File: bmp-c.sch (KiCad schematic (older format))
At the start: 66 parts, among them J1 USB_C_Receptacle_USB2.0, J2 Conn_01x10, J3 Conn_01x04, J4 JTAG-10, Q1 DMG1023DV, Q2 DMG1024UV, SW1 SW_SPST, U1 USBLC6-2SC6, U2 74LVC2T45DC, U3 74LVC2T45DC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

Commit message: Assign footprints
Signed-off-by: Dominik Sliwa <dominik@e-plum.pl>
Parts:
- C1, C10, C11, C12, C13, C14, C15, C16, C17, C18, C19, C2, C20, C4, C5, C6, C8, C9: footprint (none) -> Capacitor_SMD:C_0402_1005Metric
- C21, C3: footprint (none) -> Capacitor_SMD:C_0603_1608Metric
- C7: footprint (none) -> Capacitor_SMD:C_0201_0603Metric
- D1, Q1, Q2: footprint (none) -> Package_TO_SOT_SMD:SOT-563
- D2, D3, D4: footprint (none) -> LED_SMD:LED_0402_1005Metric
- FB1: footprint (none) -> Fuse:Fuse_0603_1608Metric
- J1: footprint (none) -> Connector_USB:USB_C_Receptacle_HRO_TYPE-C-31-M-12
- J2: footprint (none) -> Connector_FFC-FPC:Hirose_FH12-10S-0.5SH_1x10-1MP_P0.50mm_Horizontal
- J3: footprint (none) -> Connector_JST:JST_SH_SM04B-SRSS-TB_1x04-1MP_P1.00mm_Horizontal
- J4: footprint (none) -> Connector_PinHeader_1.27mm:PinHeader_2x05_P1.27mm_Vertical_SMD
- JP1, JP2, JP3: footprint (none) -> Jumper:SolderJumper-2_P1.3mm_Bridged_RoundedPad1.0x1.5mm
- JP4: footprint (none) -> Jumper:SolderJumper-2_P1.3mm_Open_RoundedPad1.0x1.5mm
- R1, R10, R11, R12, R2, R3, R4, R5, R6, R7, R8, R9: footprint (none) -> Resistor_SMD:R_0402_1005Metric
- RN1, RN2, RN3: footprint (none) -> Resistor_SMD:R_Array_Convex_4x0402
- SW1: footprint (none) -> Button_Switch_SMD:SW_SPST_B3U-1000P
- TP1, TP2, TP3, TP4, TP5, TP6: footprint (none) -> TestPoint:TestPoint_Pad_D1.0mm
- U7: footprint (none) -> Package_DFN_QFN:UDFN-4_1x1mm_P0.65mm
- Y1: footprint (none) -> Crystal:Crystal_SMD_3225-4Pin_3.2x2.5mm

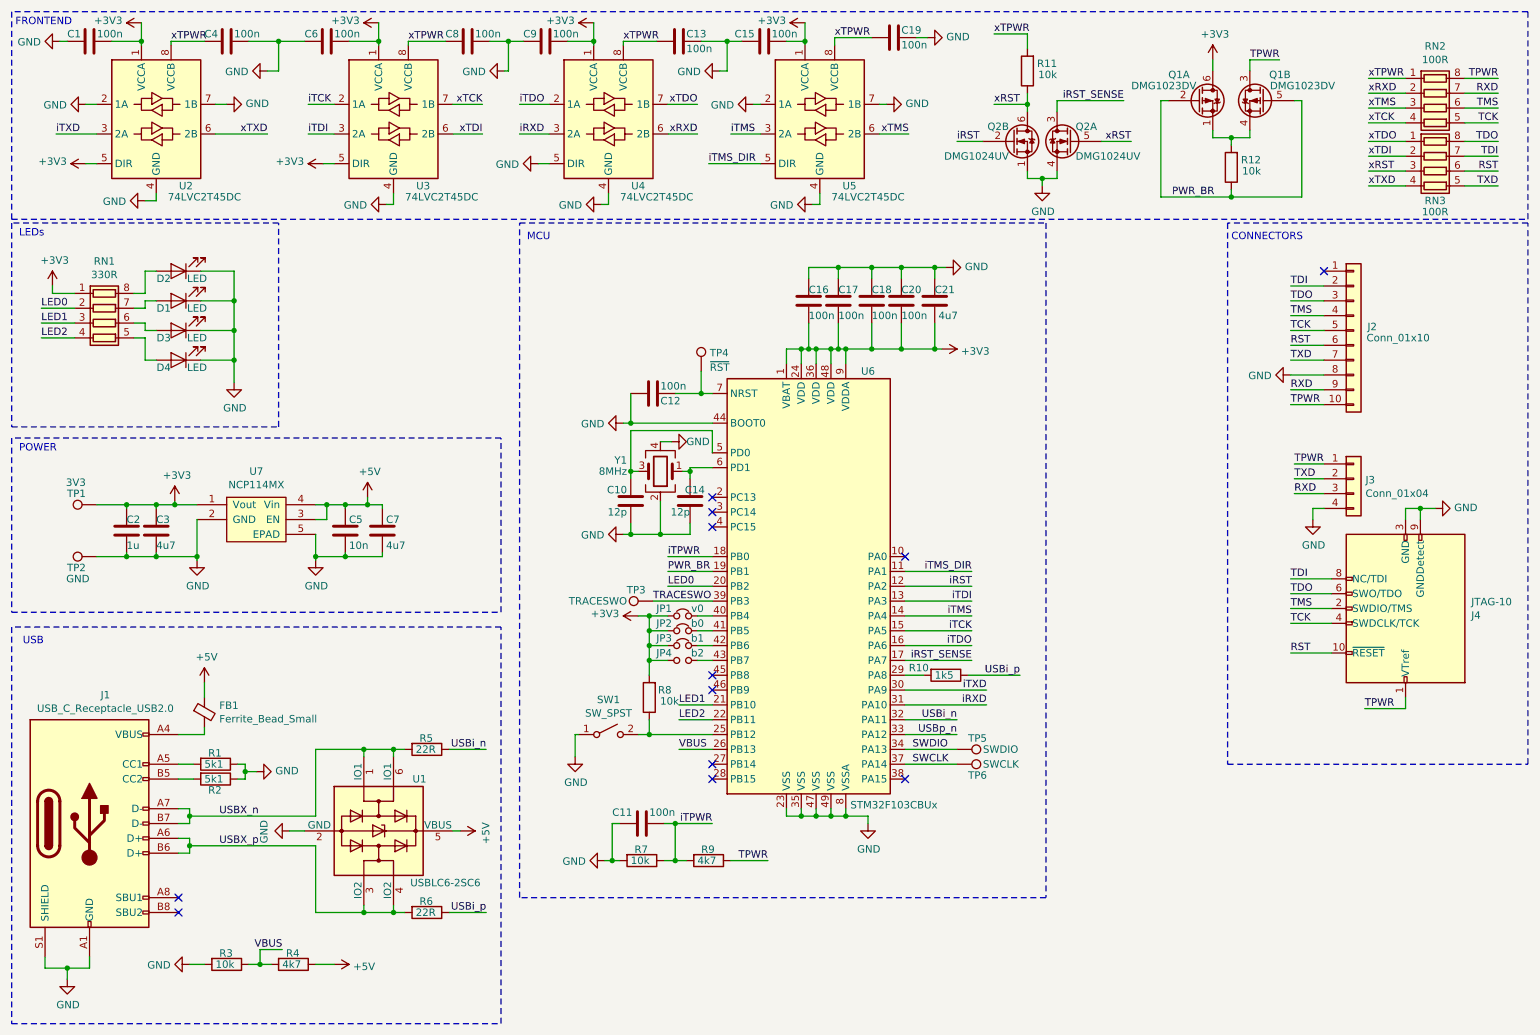
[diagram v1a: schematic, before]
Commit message: Change level-shifter package and schematic fix
-USBi_p was not conencted to the MCU
-Use 74LVC2T45 in the DSBGA8 package

Signed-off-by: Dominik Sliwa <dominik@e-plum.pl>
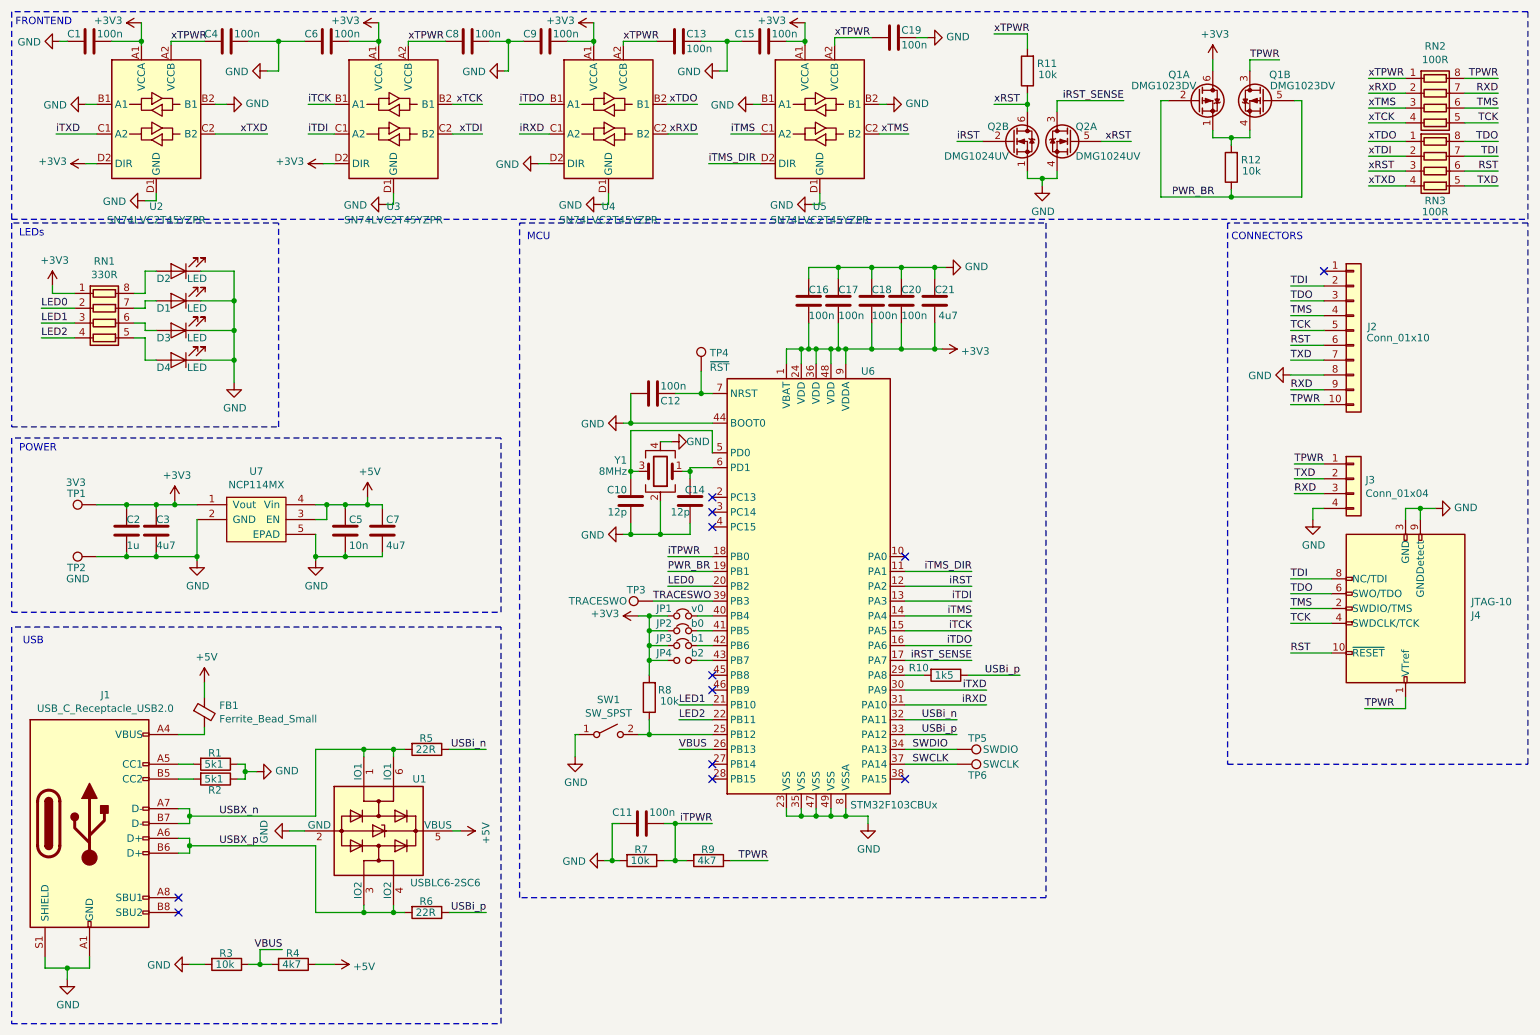
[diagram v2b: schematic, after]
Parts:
- removed U2, U3, U4, U5: 74LVC2T45DC, Package_SO:VSSOP-8_2.3x2mm_P0.5mm, symbol Logic_LevelTranslator:74LVC2T45DC
- added U2, U3, U4, U5: SN74LVC2T45YZPR, Package_BGA:Texas_DSBGA-8_0.9x1.9mm_Layout2x4_P0.5mm, symbol Logic_LevelTranslator:SN74LVC2T45YZPR
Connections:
- net USBp_n is gone; now on net USBi_p: U6.33 (PA12)
- net +3V3: now also U2.A1 (VCCA), U2.D2 (DIR), U3.A1 (VCCA), U3.D2 (DIR), U4.A1 (VCCA), U5.A1 (VCCA)
- net GND: now also U2.B1 (A1), U2.B2 (B1), U2.D1 (GND), U3.D1 (GND), U4.D1 (GND), U4.D2 (DIR), U5.B1 (A1), U5.B2 (B1), U5.D1 (GND)
- net iRXD: now also U4.C1 (A2)
- net iTCK: now also U3.B1 (A1)
- net iTDI: now also U3.C1 (A2)
- net iTDO: now also U4.B1 (A1)
- net iTMS: now also U5.C1 (A2)
- net iTMS_DIR: now also U5.D2 (DIR)
- net iTXD: now also U2.C1 (A2)
- net xRXD: now also U4.C2 (B2)
- net xTCK: now also U3.B2 (B1)
- net xTDI: now also U3.C2 (B2)
- net xTDO: now also U4.B2 (B1)
- net xTMS: now also U5.C2 (B2)
- net xTPWR: now also U2.A2 (VCCB), U3.A2 (VCCB), U4.A2 (VCCB), U5.A2 (VCCB)
- net xTXD: now also U2.C2 (B2)
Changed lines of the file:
@@
-$EndComp
-$Comp
-L Logic_LevelTranslator:74LVC2T45DC U2
-U 1 1 5D4F4469
-P 1700 1225
-F 0 "U2" H 1900 775 50  0000 C CNN
-F 1 "74LVC2T45DC" H 2025 700 50  0000 C CNN
-F 2 "Package_SO:VSSOP-8_2.3x2mm_P0.5mm" H 1700 375 50  0001 C CNN
-F 3 "https://assets.nexperia.com/documents/data-sheet/74LVC_LVCH2T45.pdf" H 1950 975 50  0001 C CNN
-	1    1700 1225
-	1    0    0    -1
-$EndComp
-$Comp
-L Logic_LevelTranslator:74LVC2T45DC U3
-U 1 1 5D4F4B29
-P 3300 1225
-F 0 "U3" H 3500 775 50  0000 C CNN
-F 1 "74LVC2T45DC" H 3625 700 50  0000 C CNN
-F 2 "Package_SO:VSSOP-8_2.3x2mm_P0.5mm" H 3300 375 50  0001 C CNN
-F 3 "https://assets.nexperia.com/documents/data-sheet/74LVC_LVCH2T45.pdf" H 3550 975 50  0001 C CNN
-	1    3300 1225
-	1    0    0    -1
-$EndComp
-$Comp
-L Logic_LevelTranslator:74LVC2T45DC U4
-U 1 1 5D4F516F
-P 4750 1225
-F 0 "U4" H 4950 775 50  0000 C CNN
-F 1 "74LVC2T45DC" H 5075 700 50  0000 C CNN
-F 2 "Package_SO:VSSOP-8_2.3x2mm_P0.5mm" H 4750 375 50  0001 C CNN
-F 3 "https://assets.nexperia.com/documents/data-sheet/74LVC_LVCH2T45.pdf" H 5000 975 50  0001 C CNN
-	1    4750 1225
-	1    0    0    -1
-$EndComp
-$Comp
-L Logic_LevelTranslator:74LVC2T45DC U5
-U 1 1 5D4F572C
-P 6175 1225
-F 0 "U5" H 6375 775 50  0000 C CNN
-F 1 "74LVC2T45DC" H 6500 700 50  0000 C CNN
-F 2 "Package_SO:VSSOP-8_2.3x2mm_P0.5mm" H 6175 375 50  0001 C CNN
-F 3 "https://assets.nexperia.com/documents/data-sheet/74LVC_LVCH2T45.pdf" H 6425 975 50  0001 C CNN
-	1    6175 1225
-	1    0    0    -1
 $EndComp
 $Comp
@@
 Wire Wire Line
 	6750 5275 7100 5275
-Wire Wire Line
-	6750 5375 7100 5375
 Text Label 7100 5275 2    50   ~ 0
 USBi_n
 Text Label 7100 5375 2    50   ~ 0
-USBp_n
+USBi_p
 $Comp
 L Connector:TestPoint TP5
@@
 Text Notes 8950 2050 0    50   ~ 0
 CONNECTORS
+$Comp
+L Logic_LevelTranslator:SN74LVC2T45YZPR U2
+U 1 1 5EC8FE70
+P 1700 1225
+F 0 "U2" H 1700 636 50  0000 C CNN
+F 1 "SN74LVC2T45YZPR" H 1700 545 50  0000 C CNN
+F 2 "Package_BGA:Texas_DSBGA-8_0.9x1.9mm_Layout2x4_P0.5mm" H 1750 675 50  0001 C CNN
+F 3 "http://www.ti.com/lit/ds/symlink/sn74lvc2t45.pdf" H 800 675 50  0001 C CNN
+	1    1700 1225
+	1    0    0    -1
+$EndComp
+$Comp
+L Logic_LevelTranslator:SN74LVC2T45YZPR U3
+U 1 1 5EC92BEC
+P 3300 1225
+F 0 "U3" H 3300 636 50  0000 C CNN
+F 1 "SN74LVC2T45YZPR" H 3300 545 50  0000 C CNN
+F 2 "Package_BGA:Texas_DSBGA-8_0.9x1.9mm_Layout2x4_P0.5mm" H 3350 675 50  0001 C CNN
+F 3 "http://www.ti.com/lit/ds/symlink/sn74lvc2t45.pdf" H 2400 675 50  0001 C CNN
+	1    3300 1225
+	1    0    0    -1
+$EndComp
+$Comp
+L Logic_LevelTranslator:SN74LVC2T45YZPR U4
+U 1 1 5EC93263
+P 4750 1225
+F 0 "U4" H 4750 636 50  0000 C CNN
+F 1 "SN74LVC2T45YZPR" H 4750 545 50  0000 C CNN
+F 2 "Package_BGA:Texas_DSBGA-8_0.9x1.9mm_Layout2x4_P0.5mm" H 4800 675 50  0001 C CNN
+F 3 "http://www.ti.com/lit/ds/symlink/sn74lvc2t45.pdf" H 3850 675 50  0001 C CNN
+	1    4750 1225
+	1    0    0    -1
+$EndComp
+$Comp
+L Logic_LevelTranslator:SN74LVC2T45YZPR U5
+U 1 1 5EC938C7
+P 6175 1225
+F 0 "U5" H 6175 636 50  0000 C CNN
+F 1 "SN74LVC2T45YZPR" H 6175 545 50  0000 C CNN
+F 2 "Package_BGA:Texas_DSBGA-8_0.9x1.9mm_Layout2x4_P0.5mm" H 6225 675 50  0001 C CNN
+F 3 "http://www.ti.com/lit/ds/symlink/sn74lvc2t45.pdf" H 5275 675 50  0001 C CNN
+	1    6175 1225
+	1    0    0    -1
+$EndComp
+Wire Wire Line
+	7100 5375 6750 5375
 $EndSCHEMATC
